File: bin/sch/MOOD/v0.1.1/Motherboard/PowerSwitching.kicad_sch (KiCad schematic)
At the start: 38 parts

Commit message: -	Made a bunch of changes -	Added KeyboardCard
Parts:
- removed SW?: SW_SPST, symbol Switch:SW_SPST
- removed U? (x2): SPX3819M5, Package_TO_SOT_SMD:SOT-23-5, symbol igor_lib:SPX3819M5
- added J13: Conn_02x01, symbol Connector_Generic:Conn_02x01
- added U11, U9: SPX3819M5-L-3-3, Package_TO_SOT_SMD:SOT-23-5, symbol Regulator_Linear:SPX3819M5-L-3-3
- added U?: LTC2955CTS8-1, TSOT-23_TS8_LIT, symbol UltraLibrarian:LTC2955xTS8-2
- C31, C33, C34, C35, C36, C37, C38, C39, C40, C41: renamed from C?; footprint (none) -> Capacitor_SMD:C_0402_1005Metric
- U5, U6, U7, U8: renamed from U?; symbol ModularDeck_Library:MAX40203ANS -> MOOD_Library:MAX40203ANS
- gave numbers to parts that had none: 20
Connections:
- net +3.3V-Supply: now also U9.5 (OUT)
- net +3.3V-Switched: now also U11.5 (OUT)
- net +5V-Supply: now also U9.1 (IN), U9.3 (EN)
- net +5V-Switched: now also U11.1 (IN), U11.3 (EN)
- net GND: now also J13.1 (Pin_1), U11.2 (GND), U9.2 (GND)
- net WOL_INT: now also J13.2 (Pin_2)
- no-connect marks 2 -> 4
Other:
- note added: "Inputs: - Power button on/off = PB - Wake-on-LAN on = ??? ( WOL NOR 5V-switch OR PB) - MCU off = KILL - Auto-on/auto-off = ON"
- note added: "On/Off Button Pin Header"
- note removed: "On/Off Button"
- moved on the sheet: C42, C43

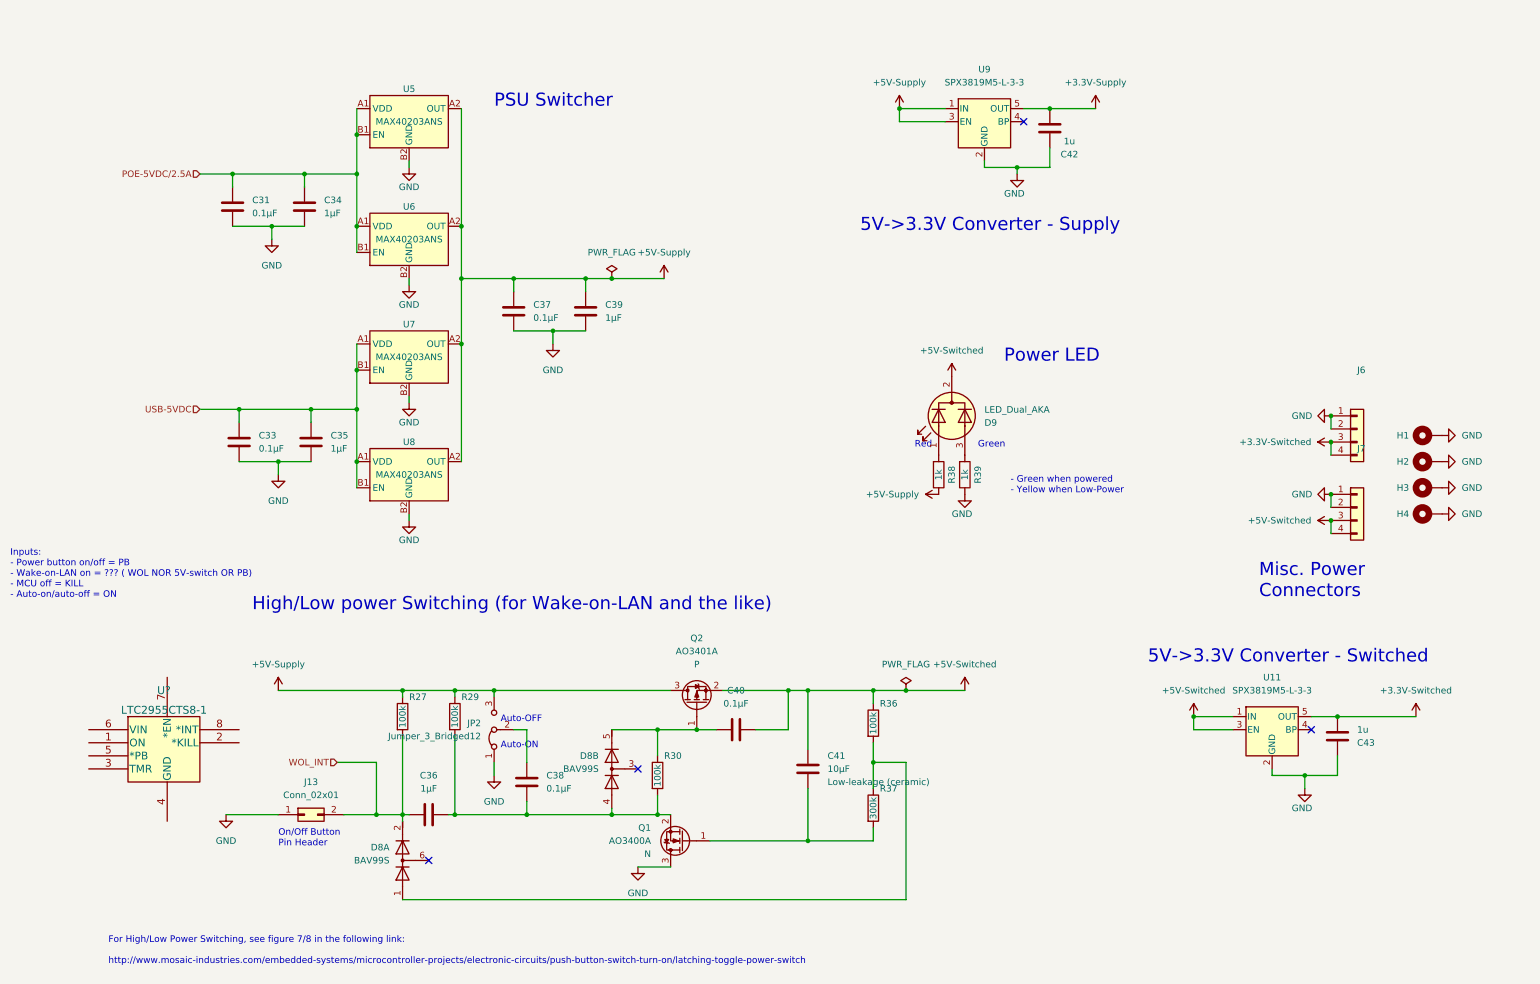
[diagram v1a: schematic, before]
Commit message: Redid power switching
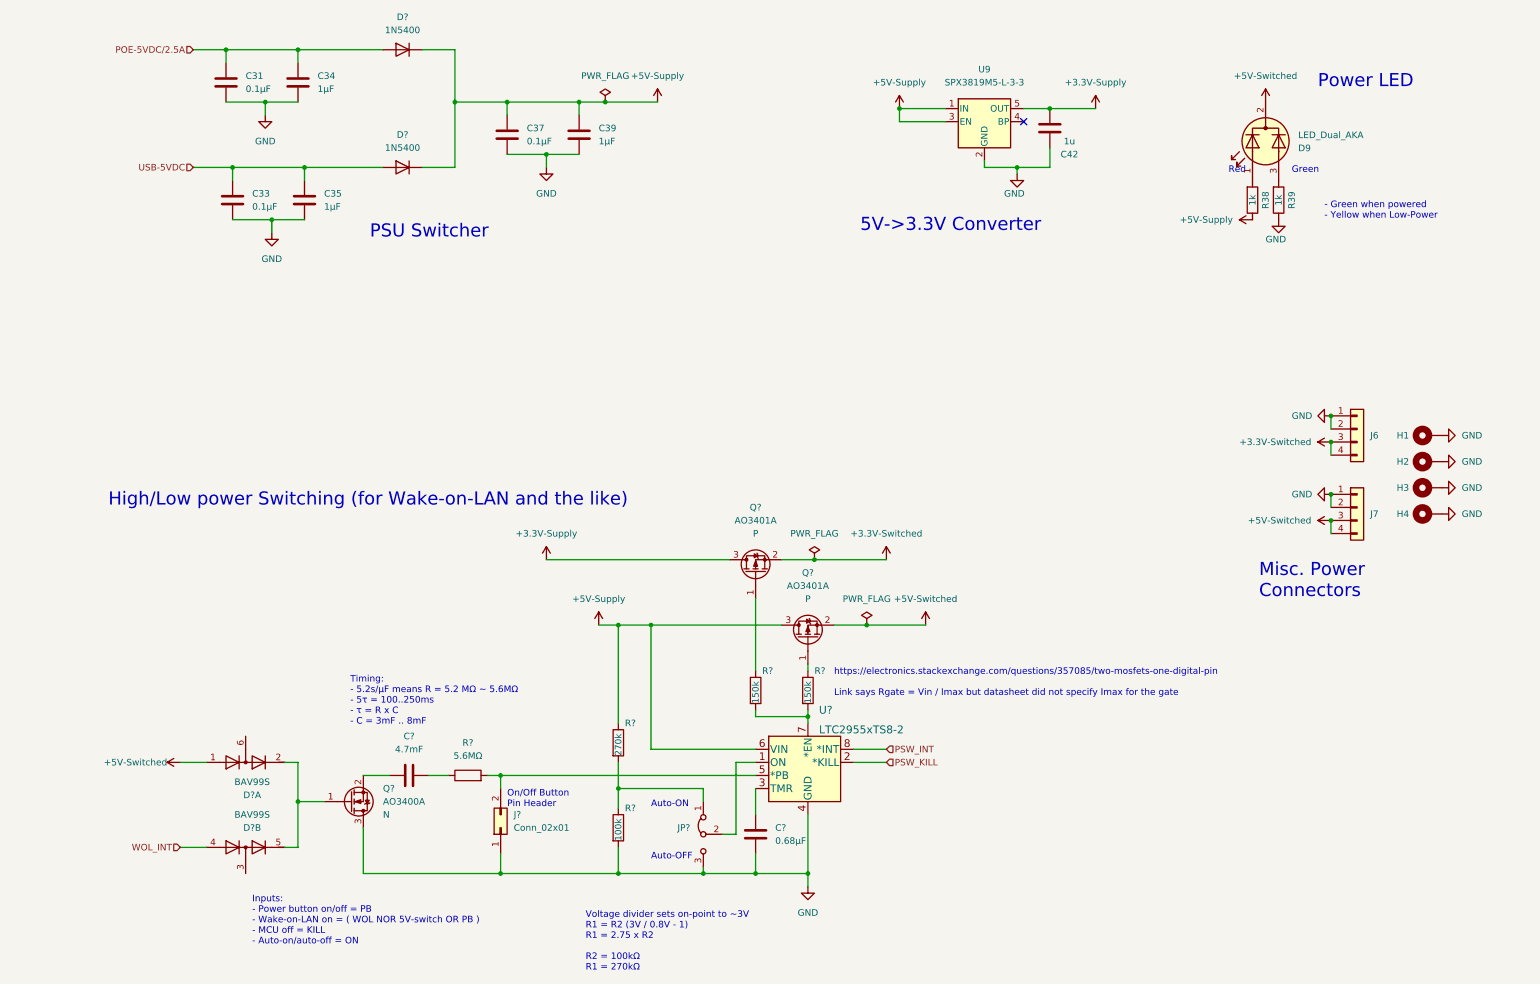
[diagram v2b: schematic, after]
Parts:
- removed C36: 1μF, Capacitor_SMD:C_0402_1005Metric, symbol Device:C
- removed C38, C40: 0.1μF, Capacitor_SMD:C_0402_1005Metric, symbol Device:C
- removed C41: 10μF, Capacitor_SMD:C_0402_1005Metric, symbol Device:C
- removed C43: 1u, Capacitor_SMD:C_0402_1005Metric, symbol Device:C
- removed D8: BAV99S, Package_TO_SOT_SMD:SOT-363_SC-70-6, symbol Diode:BAV99S
- removed J13: Conn_02x01, symbol Connector_Generic:Conn_02x01
- removed JP2: Jumper_3_Bridged12, symbol Jumper:Jumper_3_Bridged12
- removed Q1: AO3400A, Package_TO_SOT_SMD:SOT-23, symbol Transistor_FET:AO3400A
- removed Q2: AO3401A, Package_TO_SOT_SMD:SOT-23, symbol Transistor_FET:AO3401A
- removed R27, R29, R30, R36: 100k, symbol Device:R
- removed R37: 300k, symbol Device:R
- removed U11: SPX3819M5-L-3-3, Package_TO_SOT_SMD:SOT-23-5, symbol Regulator_Linear:SPX3819M5-L-3-3
- removed U5, U6, U7, U8: MAX40203ANS, Package_BGA:WLP-4_0.73x0.73mm_Layout2x2_P0.35mm_Ball0.22mm_Pad0.2mm_NSMD, symbol MOOD_Library:MAX40203ANS
- added C?: 0.68μF, symbol Device:C
- added C?: 4.7mF, symbol Device:C
- added D? (x2): BAV99S, Package_TO_SOT_SMD:SOT-363_SC-70-6, symbol Diode:BAV99S
- added D? (x2): 1N5400, Diode_THT:D_DO-201AD_P15.24mm_Horizontal, symbol Diode:1N5400
- added J?: Conn_02x01, symbol Connector_Generic:Conn_02x01
- added JP?: Jumper_3_Bridged12, symbol Jumper:Jumper_3_Bridged12
- added Q? (x2): AO3401A, Package_TO_SOT_SMD:SOT-23, symbol Transistor_FET:AO3401A
- added Q?: AO3400A, Package_TO_SOT_SMD:SOT-23, symbol Transistor_FET:AO3400A
- added R? (x2): 150k, symbol Device:R
- added R?: 100k, symbol Device:R
- added R?: 270k, symbol Device:R
- added R?: 5.6MΩ, symbol Device:R
- U?: value LTC2955CTS8-1 -> LTC2955xTS8-2
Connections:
- net +3.3V-Supply: now also Q?.3 (D)
- net +3.3V-Switched: now also Q?.2 (S)
- net +5V-Supply: now also U?.6 (VIN), D?.1 (K), D?.1 (K), Q?.3 (D), R?.1
- net +5V-Switched: now also D?.1 (A1), Q?.2 (S)
- net GND: now also U?.4 (GND), C?.2, J?.1 (Pin_1), JP?.3 (B), Q?.3 (D), R?.2
- net POE-5VDC/2.5A: now also D?.2 (A)
- net USB-5VDC: now also D?.2 (A)
- net WOL_INT: now also D?.4 (A3)
- net at U?.1 (ON): now also JP?.2 (C)
- net PSW_KILL: now reaches U?.2 (*KILL)
- net at U?.3 (TMR): now also C?.1
- net at U?.5 (*PB): now also J?.2 (Pin_2), R?.2
- net at U?.7 (*EN): now also R?.2, R?.2
- net PSW_INT: now reaches U?.8 (*INT)
- new net: Q?.1 (G), R?.1 (x2)
- new net: JP?.1 (A), R?.1, R?.2
- new net: C?.2, R?.1
- new net: D?.2 (K2), D?.5 (K4), Q?.1 (G)
- new net: C?.1, Q?.2 (S)
- no-connect marks 4 -> 1
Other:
- note added: "5V->3.3V Converter"
- note added: "Inputs: - Power button on/off = PB - Wake-on-LAN on = ( WOL NOR 5V-switch OR PB ) - MCU off = KILL - Auto-on/auto-off = ON"
- note added: "Timing: - 5.2s/μF means R = 5.2 MΩ ~ 5.6MΩ - 5τ = 100..250ms - τ = R x C - C = 3mF .. 8mF"
- note added: "Voltage divider sets on-point to ~3V R1 = R2 (3V / 0.8V - 1) R1 = 2.75 x R2 R2 = 100kΩ R1 = 270kΩ"
- note added: "https://electronics.stackexchange.com/questions/357085/two-mosfets-one-digital-pin Link says Rgate = Vin / Imax but datasheet did not specify Imax for the gate"
- note removed: "5V->3.3V Converter - Supply"
- note removed: "5V->3.3V Converter - Switched"
- note removed: "For High/Low Power Switching, see figure 7/8 in the following link: http://www.mosaic-industries.com/embedded-systems/microcontroller-projects/electronic-circuits/push-button-switch-turn-on/latching-toggle-power-switch"
- note removed: "Inputs: - Power button on/off = PB - Wake-on-LAN on = ??? ( WOL NOR 5V-switch OR PB) - MCU off = KILL - Auto-on/auto-off = ON"
- moved on the sheet: C31, C33, C34, C35, C37, C39, D9, R38, R39, U?

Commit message: -	Hopefully finished schematics -	Started desining PCB for motherboard
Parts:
- added J14: Conn_02x01, symbol Connector_Generic:Conn_02x01
- added R3, R4: 130k, symbol Device:R
- U1: renamed from U?; Note (none) -> LTC2952 seems attractive, but doesn't allow for WOL
- gave numbers to parts that had none: 15
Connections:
- net +5V-Supply: now also J14.2 (Pin_2)
- net +5V-Switched: now also R3.1
- net GND: now also R3.2, R4.1
- net PSW_KILL: now also J14.1 (Pin_1)
- net WOL_INT: now also R4.2
- no-connect marks 1 -> 3
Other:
- note added: "*KILL override pin header Pin Header"
- note added: "Pull-down resistors: - AO3400A Gate Threshold Voltage Min: 0.65V - Rmax = Vil(max) / Iil - Rmax = 0.65V / 1-5μA - R = 130-650kΩ Since a smaller resistor ties more strongly to the rail, We use 130k"
- moved on the sheet: C36, C38, D1A, D1B, J13, JP2, Q1, Q2, Q3, R27, R29, R30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

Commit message: Finalised schematic and PCB for MOOD Motherboard
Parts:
- C36, C38: footprint (none) -> Capacitor_SMD:C_0402_1005Metric
- D9: footprint (none) -> LED_SMD:LED-L1T2_LUMILEDS
- J13: value Conn_02x01 -> On/Off Button; footprint (none) -> Connector_PinHeader_2.54mm:PinHeader_2x01_P2.54mm_Vertical
- J14: value Conn_02x01 -> Kill Override; footprint (none) -> Connector_PinHeader_2.54mm:PinHeader_2x01_P2.54mm_Vertical
- JP2: footprint (none) -> Connector_PinHeader_2.54mm:PinHeader_1x03_P2.54mm_Vertical
- R27, R29, R3, R30, R36, R4, R5: footprint (none) -> Resistor_SMD:R_0402_1005Metric
- U1: footprint TSOT-23_TS8_LIT -> Package_TO_SOT_SMD:TSOT-23-8
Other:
- note removed: "On/Off Button Pin Header"
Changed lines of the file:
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@@
     (stroke (width 0) (type default) (color 0 0 0 0))
-  )
-  (text "On/Off Button\nPin Header" (at 106.68 162.56 0)
-    (effects (font (size 1.27 1.27)) (justify left bottom))
   )
   (text "Green" (at 245.11 41.91 0)
@@
     (effects (font (size 2.54 2.54)) (justify left bottom))
   )
-  (text "*KILL override pin header\nPin Header" (at 208.28 147.32 0)
+  (text "*KILL override pin header\nPin Header" (at 210.82 147.32 0)
     (effects (font (size 1.27 1.27)) (justify left bottom))
   )
@@
       (effects (font (size 1.27 1.27)) (justify left))
     )
-    (property "Footprint" "" (id 2) (at 155.9052 171.45 0)
+    (property "Footprint" "Capacitor_SMD:C_0402_1005Metric" (id 2) (at 155.9052 171.45 0)
       (effects (font (size 1.27 1.27)) hide)
     )
@@
       (effects (font (size 1.27 1.27)) (justify right))
     )
-    (property "Value" "Conn_02x01" (id 1) (at 205.74 148.5899 90)
+    (property "Value" "Kill Override" (id 1) (at 205.74 148.5899 90)
       (effects (font (size 1.27 1.27)) (justify right))
     )
-    (property "Footprint" "" (id 2) (at 203.2 148.59 0)
+    (property "Footprint" "Connector_PinHeader_2.54mm:PinHeader_2x01_P2.54mm_Vertical" (id 2) (at 203.2 148.59 0)
       (effects (font (size 1.27 1.27)) hide)
     )
@@
     )
     (property "Value" "130k" (id 1) (at 46.99 166.37 90))
-    (property "Footprint" "" (id 2) (at 45.212 166.37 90)
+    (property "Footprint" "Resistor_SMD:R_0402_1005Metric" (id 2) (at 45.212 166.37 90)
       (effects (font (size 1.27 1.27)) hide)
     )
@@
       (effects (font (size 1.27 1.27)) (justify left))
     )
-    (property "Footprint" "" (id 2) (at 163.322 139.7 90)
+    (property "Footprint" "Resistor_SMD:R_0402_1005Metric" (id 2) (at 163.322 139.7 90)
       (effects (font (size 1.27 1.27)) hide)
     )
@@
       (effects (font (size 1.27 1.27)) (justify left))
     )
-    (property "Footprint" "" (id 2) (at 126.492 166.37 90)
+    (property "Footprint" "Resistor_SMD:R_0402_1005Metric" (id 2) (at 126.492 166.37 90)
       (effects (font (size 1.27 1.27)) hide)
     )
@@
       (effects (font (size 1.27 1.27)) (justify right))
     )
-    (property "Footprint" "" (id 2) (at 240.03 35.56 0)
+    (property "Footprint" "LED_SMD:LED-L1T2_LUMILEDS" (id 2) (at 240.03 35.56 0)
       (effects (font (size 1.27 1.27)) hide)
     )
@@
       (effects (font (size 1.27 1.27)) (justify left))
     )
-    (property "Footprint" "" (id 2) (at 126.492 149.86 90)
+    (property "Footprint" "Resistor_SMD:R_0402_1005Metric" (id 2) (at 126.492 149.86 90)
       (effects (font (size 1.27 1.27)) hide)
     )
@@
     (property "Reference" "R5" (id 0) (at 99.06 149.86 90))
     (property "Value" "5.6MΩ" (id 1) (at 99.06 152.4 90))
-    (property "Footprint" "" (id 2) (at 99.06 157.988 90)
+    (property "Footprint" "Resistor_SMD:R_0402_1005Metric" (id 2) (at 99.06 157.988 90)
       (effects (font (size 1.27 1.27)) hide)
     )
@@
       (effects (font (size 1.27 1.27)) (justify right))
     )
-    (property "Value" "Conn_02x01" (id 1) (at 107.95 166.3699 90)
+    (property "Value" "On/Off Button" (id 1) (at 107.95 166.3699 90)
       (effects (font (size 1.27 1.27)) (justify right))
     )
-    (property "Footprint" "" (id 2) (at 105.41 166.37 0)
+    (property "Footprint" "Connector_PinHeader_2.54mm:PinHeader_2x01_P2.54mm_Vertical" (id 2) (at 105.41 166.37 0)
       (effects (font (size 1.27 1.27)) hide)
     )
@@
       (effects (font (size 1.524 1.524)) (justify left))
     )
-    (property "Footprint" "TSOT-23_TS8_LIT" (id 2) (at 177.8 135.89 0)
+    (property "Footprint" "Package_TO_SOT_SMD:TSOT-23-8" (id 2) (at 177.8 135.89 0)
       (effects (font (size 1.524 1.524)) hide)
     )
@@
     (property "Reference" "C36" (id 0) (at 87.63 148.59 90))
     (property "Value" "4.7mF" (id 1) (at 87.63 151.13 90))
-    (property "Footprint" "" (id 2) (at 91.44 155.2448 0)
+    (property "Footprint" "Capacitor_SMD:C_0402_1005Metric" (id 2) (at 91.44 155.2448 0)
       (effects (font (size 1.27 1.27)) hide)
     )
@@
     )
     (property "Value" "130k" (id 1) (at 46.99 156.21 90))
-    (property "Footprint" "" (id 2) (at 45.212 156.21 90)
+    (property "Footprint" "Resistor_SMD:R_0402_1005Metric" (id 2) (at 45.212 156.21 90)
       (effects (font (size 1.27 1.27)) hide)
     )
@@
       (effects (font (size 1.27 1.27)) (justify left))
     )
-    (property "Footprint" "" (id 2) (at 153.162 139.7 90)
+    (property "Footprint" "Resistor_SMD:R_0402_1005Metric" (id 2) (at 153.162 139.7 90)
       (effects (font (size 1.27 1.27)) hide)
     )
@@
       (effects (font (size 1.27 1.27)) (justify left) hide)
     )
-    (property "Footprint" "" (id 2) (at 144.78 167.64 0)
+    (property "Footprint" "Connector_PinHeader_2.54mm:PinHeader_1x03_P2.54mm_Vertical" (id 2) (at 144.78 167.64 0)
       (effects (font (size 1.27 1.27)) hide)
     )
@@
       (effects (font (size 1.27 1.27)) hide)
     )
-    (pin "1")
-    (pin "2")
+    (property "Description" "Auto-Off/On" (id 4) (at 144.78 167.64 90))
+    (pin "1")
+    (pin "2")
